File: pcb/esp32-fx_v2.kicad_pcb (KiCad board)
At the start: 4 copper layers, 48 x 95 mm, 80 parts, among them J1 AudioJack2 (out), J2 AudioJack2 (in), K1 G6E-134P-US-DC3, P1 USB_C_Plug_USB2.0, Q1 MMBT2222A, SW1 SW_Push, U1 ESP32-S3-WROOM-1, U10 OPA1655DBV, U11 D3V3XA4B10LP, U2 TPD1E05U06DYA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

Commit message: added images of pcb
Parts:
- removed the C17 at (150.8, 88.4)
- moved R1 1.40 mm to (150.8, 88.5)
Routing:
- net /U3A-OUT: track 18.9 -> 17.4 mm
- net Net-(U10-+): track 20.7 -> 19.4 mm
- net GND: vias 131 -> 132
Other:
- board text removed: "BLCK"
- board text removed: "DIN"
- board text removed: "DOUT"
- board text removed: "LRCKL"
- board text removed: "MLCK"
- board text removed: "NRST"
- board text removed: "SCL"
- board text removed: "SDA"

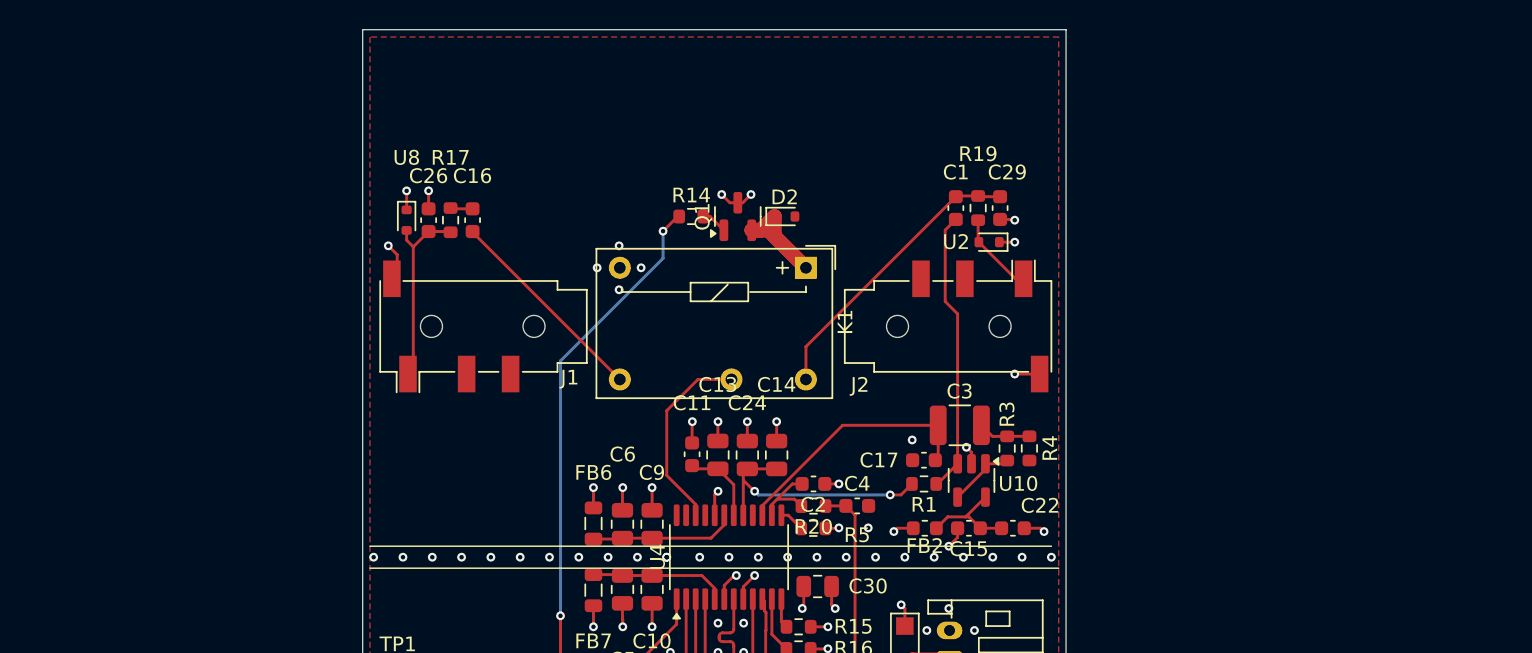
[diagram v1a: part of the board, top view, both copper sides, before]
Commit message: fixed input and output values and removed opamp
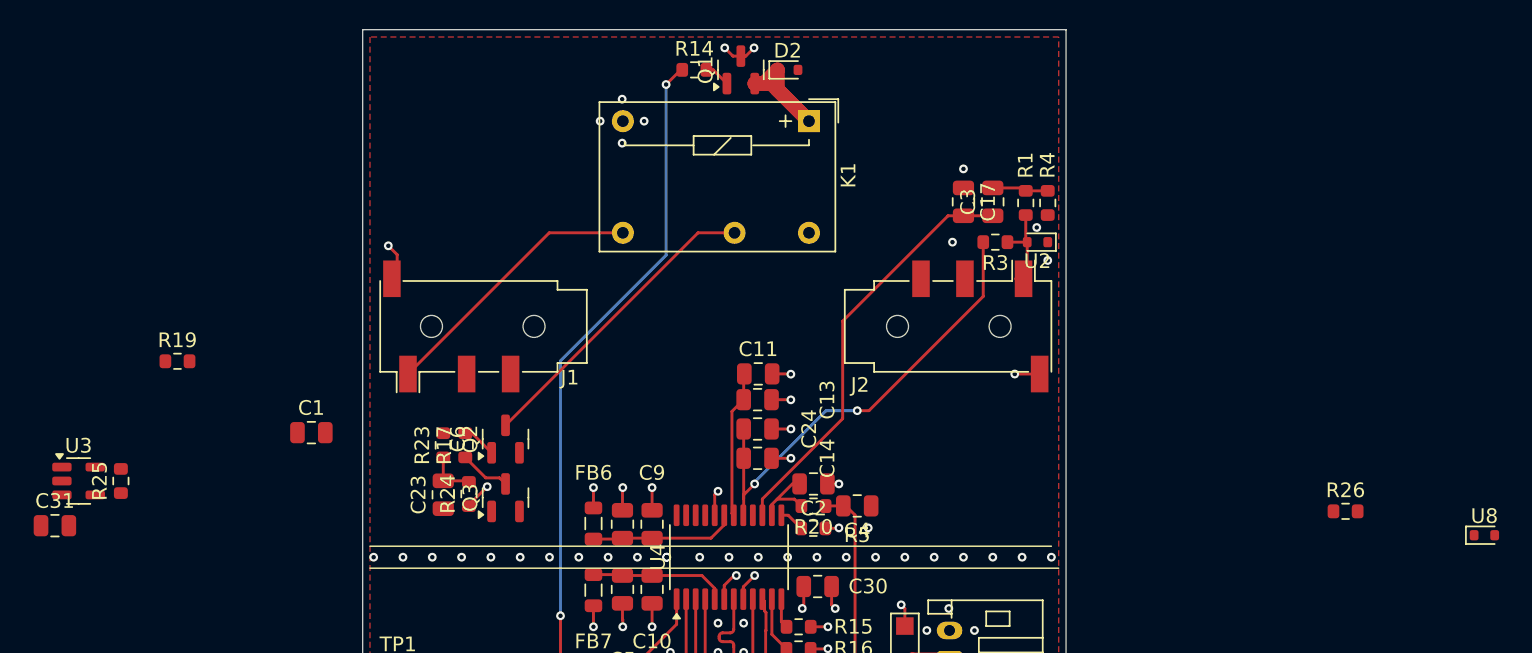
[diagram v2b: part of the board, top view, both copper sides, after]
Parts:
- removed C15, C16: 1uf, Capacitor_SMD:C_0603_1608Metric
- removed C22: 0.1uf, Capacitor_SMD:C_0603_1608Metric
- removed C26: 100pf, Capacitor_SMD:C_0603_1608Metric
- removed C29: 100nf, Capacitor_SMD:C_0603_1608Metric
- removed FB2: 600 Ω 0.06 Ω, Inductor_SMD:L_0603_1608Metric
- removed U10: OPA1655DBV, Package_TO_SOT_SMD:SOT-23-5
- added C23: 3.3uf, Capacitor_SMD:C_0805_2012Metric, F.Cu at (118.0, 89.2)
- added C31: 3.3uf, Capacitor_SMD:C_0805_2012Metric, F.Cu at (91.5, 91.3)
- added Q2: MMBT2222A, Package_TO_SOT_SMD:SOT-23, F.Cu at (122.2, 85.4)
- added Q3: MMUN2111LT1, Package_TO_SOT_SMD:SOT-23, F.Cu at (122.2, 89.4)
- added R23: 470, Resistor_SMD:R_0603_1608Metric, F.Cu at (118.0, 85.9)
- added R24: 10k, Resistor_SMD:R_0603_1608Metric, F.Cu at (119.8, 89.2)
- added R25: 10k, Resistor_SMD:R_0603_1608Metric, F.Cu at (96.0, 88.3)
- added R26: 47k, Resistor_SMD:R_0603_1608Metric, F.Cu at (179.6, 90.4)
- added U3: OPA333xxDBV, Package_TO_SOT_SMD:SOT-23-5, F.Cu at (93.1, 88.3)
- C1: value 1uf -> 1uF; footprint Capacitor_SMD:C_0603_1608Metric -> Capacitor_SMD:C_0805_2012Metric
- C11, C17, C2, C4: footprint Capacitor_SMD:C_0603_1608Metric -> Capacitor_SMD:C_0805_2012Metric
- C3: footprint Capacitor_SMD:C_1210_3225Metric -> Capacitor_SMD:C_0805_2012Metric
- R1: value 100k -> 2k
- R17: value 22 -> 2k
- R19: value 1k -> 560
- R3: value 2k -> 100k
- moved U8 76.6 mm to (189.1, 92.0), turned to 0 degrees
- moved R19 55.6 mm to (99.9, 80.1), turned to 0 degrees
- moved C1 46.6 mm to (109.0, 85.0), turned to 0 degrees
- moved R1 20.4 mm to (157.8, 69.3), turned to -90 degrees
- moved C17 17.8 mm to (153.5, 69.2), turned to -90 degrees
- moved R4 16.8 mm to (159.2, 69.3)
- moved C3 15.4 mm to (155.5, 69.2), turned to 90 degrees
- moved R17 15.4 mm to (119.5, 85.9), turned to 90 degrees
- moved R3 14.1 mm to (155.7, 72.0), turned to 180 degrees
- moved D2 10.0 mm to (141.5, 60.2)
- moved K1 10.0 mm to (143.0, 63.7)
- moved Q1 10.0 mm to (138.3, 60.2)
- moved R14 10.0 mm to (135.1, 60.2)
- moved C11 7.10 mm to (139.5, 81.0), turned to 0 degrees
- moved C13 4.64 mm to (139.4, 82.8), turned to 180 degrees
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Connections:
- C1 pad 1: Net-(U10-+) -> Net-(C1-Pad1)
- C1 pad 2: /audioINjack -> Net-(C1-Pad2)
- C27 pad 1: Net-(C27-Pad1) -> GND
- C28 pad 1: Net-(U7-VO) -> +3.3V
- C28 pad 2: +3.3V -> GND
- FB5 pad 2: Net-(C27-Pad1) -> Net-(U7-VI)
- J1 pad T: Net-(U8-GND) -> /audioOUTjack
- R1 pad 1: Net-(U10-+) -> Net-(C3-Pad2)
- R1 pad 2: /VQ -> Net-(U2-GND)
- R17 pad 2: Net-(U8-GND) -> Net-(Q2-B)
- R19 pad 1: Net-(U2-GND) -> Net-(C1-Pad2)
- R19 pad 2: /audioINjack -> /AudioOUT
- R3 pad 1: Net-(U10--) -> Net-(U2-GND)
- R3 pad 2: Net-(C3-Pad2) -> /VQ
- U4 pad 21: unconnected-(U4-~{MUTEA}-Pad21) -> /MUTE
- U4 pad 22: /AudioOUT -> Net-(U4-OUTA)
- U7 pad 2: Net-(U7-VO) -> +3.3V
- U8 pad 2: Net-(U8-GND) -> /audioOUTjack
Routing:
- net /audioINjack: track 19.8 -> 0.00 mm
- net Net-(U10-+): track 19.4 -> 0.00 mm
- net /VQ: track 17.5 -> 31.9 mm
- net Net-(U8-GND): track 13.0 -> 0.00 mm
- net /U3A-OUT: track 17.4 -> 28.7 mm
- net /relay: track 67.7 -> 77.8 mm
- net /AudioOUT: track 13.3 -> 21.1 mm
- net Net-(U10-V+): track 7.00 -> 0.00 mm
- net GND: track 79.2 -> 72.2 mm, vias 132 -> 129
- net Net-(U10--): track 4.63 -> 0.00 mm
- net Net-(U4-FIL+): track 5.47 -> 10.1 mm
- net /audioOUTjack: track 14.3 -> 18.7 mm
- net Net-(C23-Pad2): track 0.00 -> 3.38 mm
- net Net-(Q2-B): track 0.00 -> 2.35 mm
- net Net-(Q3-C): track 1.52 -> 3.50 mm
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- removed copper zone on F.Cu, net Net-(U7-VO)

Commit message: added mute layout
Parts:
- C11: value 47uf -> 10uf; footprint Capacitor_SMD:C_0805_2012Metric -> Capacitor_SMD:C_0603_1608Metric
- C13, C14: footprint Capacitor_SMD:C_0805_2012Metric -> Capacitor_SMD:C_0603_1608Metric
- C24: value 10uF -> 47uF; footprint Capacitor_SMD:C_0805_2012Metric -> Capacitor_SMD:C_0603_1608Metric
- moved U8 74.1 mm to (115.5, 83.5), turned to 180 degrees
- moved R26 56.1 mm to (123.8, 84.0)
- moved C31 32.5 mm to (124.0, 89.7), turned to -90 degrees
- moved U3 27.7 mm to (120.8, 90.2)
- moved R25 21.9 mm to (117.8, 91.0), turned to -90 degrees
- moved R19 20.2 mm to (119.6, 84.2)
- moved C23 15.1 mm to (132.8, 86.2)
- moved R23 13.1 mm to (131.1, 86.2), turned to -90 degrees
- moved D2 10.5 mm to (141.5, 70.7)
- moved K1 10.5 mm to (143.0, 74.2)
- moved Q1 10.5 mm to (138.3, 70.7)
- moved R14 10.5 mm to (135.1, 70.7)
- moved R24 10.2 mm to (129.5, 86.2), turned to -90 degrees
- moved C1 10.1 mm to (118.9, 86.7), turned to 90 degrees
- moved C11 6.35 mm to (136.0, 86.3), turned to 90 degrees
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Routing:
- net /LPF: track 0.00 -> 14.4 mm
- net Net-(Q3-C): track 3.50 -> 16.2 mm, vias 0 -> 2
- net /MUTE: track 0.00 -> 12.3 mm, vias 0 -> 2
- net /relay: track 77.8 -> 67.3 mm
- net /MUTE+: track 0.00 -> 6.44 mm, vias 0 -> 2
- net Net-(U4-OUTA): track 0.00 -> 5.33 mm
- net Net-(U4-FIL+): track 10.1 -> 5.41 mm
- net /VQ: track 31.9 -> 29.6 mm
- net /AudioOUT: track 21.1 -> 19.0 mm
- net GND: track 72.2 -> 70.2 mm, vias 129 -> 128
- net Net-(Q2-B): track 2.35 -> 4.33 mm
- net Net-(C1-Pad1): track 0.00 -> 1.88 mm
- net /MUTE-: track 0.00 -> 1.86 mm
- net Net-(C1-Pad2): track 0.00 -> 1.77 mm
- net /audioOUTjack: track 18.7 -> 19.5 mm
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
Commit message: added back opamp
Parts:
- removed R3: 100k, Resistor_SMD:R_0603_1608Metric
- added C15: 0.1uF, Capacitor_SMD:C_0805_2012Metric, F.Cu at (152.5, 91.5)
- added C16: 1uF, Capacitor_SMD:C_0805_2012Metric, F.Cu at (152.5, 89.5)
- added FB1: 100 Ω at 100 MHz, Inductor_SMD:L_0805_2012Metric, F.Cu at (149.9, 90.5)
- added U9: OPA333xxDBV, Package_TO_SOT_SMD:SOT-23-5, F.Cu at (152.5, 86.8)
- moved C17 22.5 mm to (156.8, 91.5), turned to 180 degrees
- moved C3 20.3 mm to (156.8, 89.5), turned to 0 degrees
- moved R4 18.6 mm to (156.8, 87.8), turned to 180 degrees
- moved R1 17.0 mm to (156.8, 86.2), turned to 180 degrees
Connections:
- net /VQ renamed Net-(U4-VQ)
- C17 pad 2: /U3A-OUT -> Net-(U9-+)
- C3 pad 1: /U3A-OUT -> Net-(U9-+)
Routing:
- net Net-(U4-VQ): track 29.6 -> 6.70 mm, vias 2 -> 0
- net /U3A-OUT: track 28.7 -> 17.3 mm
- net Net-(U2-GND): track 5.95 -> 15.1 mm
- net Net-(U9-+): track 0.00 -> 7.00 mm
- net GND: track 70.2 -> 73.7 mm, vias 128 -> 131
- net +3.3V: track 53.9 -> 55.6 mm, vias 18 -> 19
- net Net-(C3-Pad2): track 3.83 -> 3.30 mm

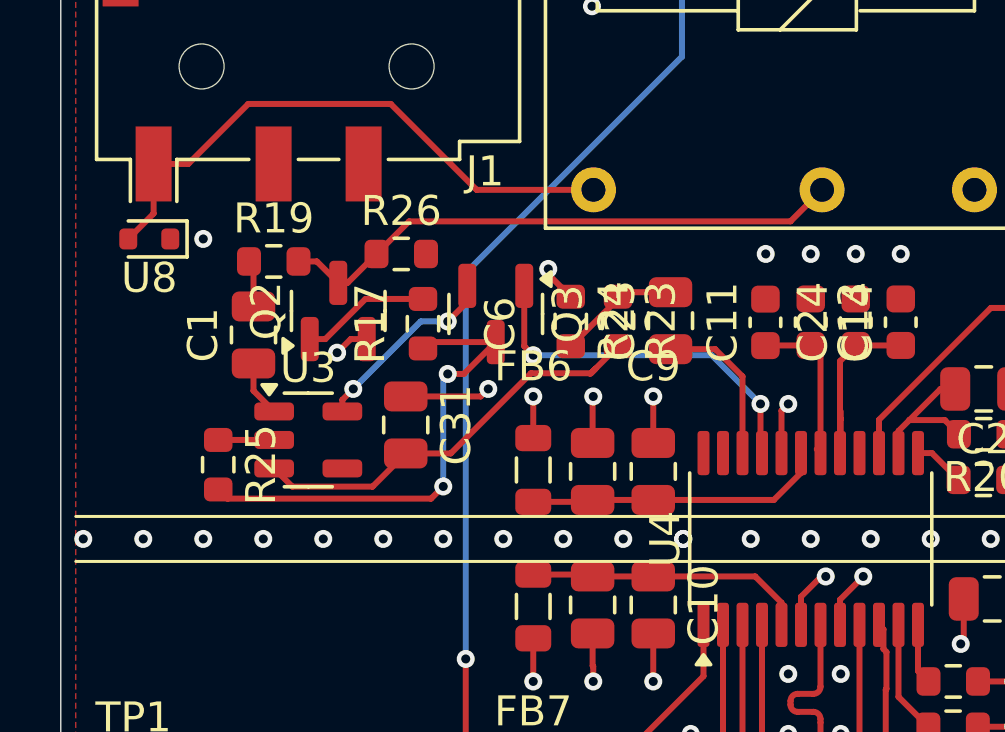
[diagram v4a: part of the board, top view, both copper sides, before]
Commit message: made opamps neater
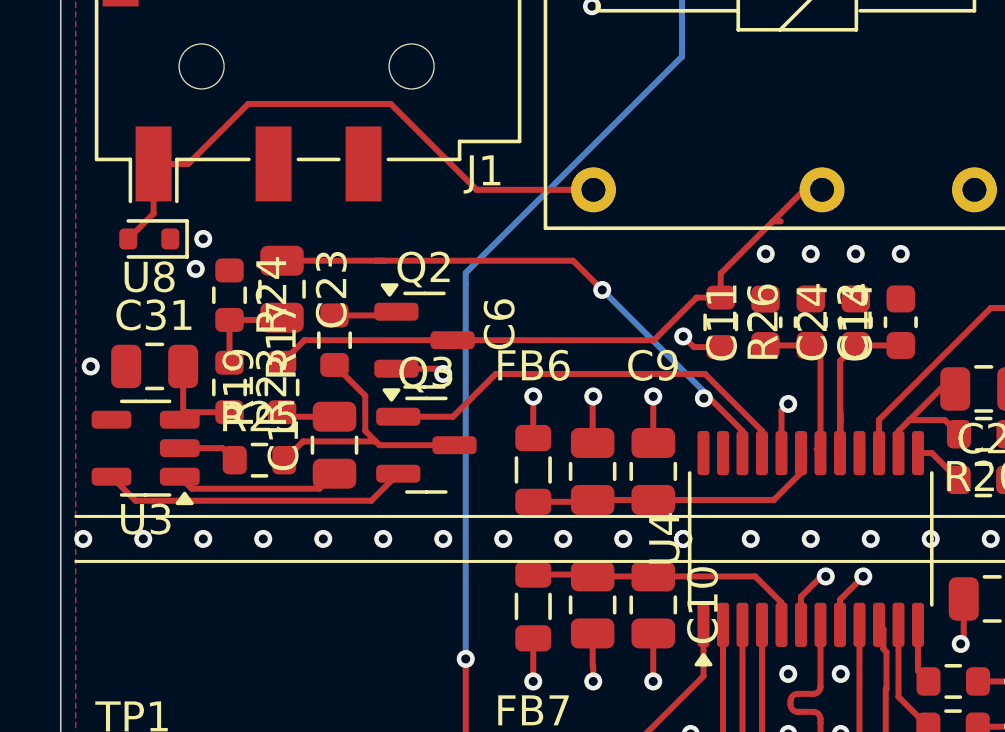
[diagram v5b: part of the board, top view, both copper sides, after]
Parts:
- moved R23 13.1 mm to (118.1, 88.5)
- moved C23 13.0 mm to (119.9, 85.2), turned to -90 degrees
- moved R24 11.4 mm to (118.1, 85.4)
- moved R26 10.9 mm to (134.5, 86.3), turned to -90 degrees
- moved C31 8.59 mm to (115.6, 87.7), turned to 0 degrees
- moved U3 5.43 mm to (115.3, 90.5), turned to 180 degrees
- moved Q3 4.95 mm to (124.7, 90.4), turned to 0 degrees
- moved C1 4.56 mm to (121.6, 90.4)
- moved R19 4.21 mm to (119.9, 88.5), turned to 90 degrees
- moved Q2 3.04 mm to (124.6, 86.9), turned to 0 degrees
- moved R17 3.00 mm to (121.6, 86.9)
- moved R25 1.38 mm to (119.1, 90.9), turned to 0 degrees
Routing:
- net Net-(U4-OUTA): track 5.33 -> 18.8 mm, vias 0 -> 2
- net /LPF: track 14.4 -> 3.58 mm
- net Net-(Q3-C): track 16.2 -> 9.11 mm, vias 2 -> 0
- net /MUTE+: track 6.44 -> 10.3 mm, vias 2 -> 0
- net Net-(C1-Pad1): track 1.88 -> 5.53 mm
- net GND: track 73.7 -> 71.5 mm, vias 131 -> 132
- net Net-(Q2-B): track 4.33 -> 2.11 mm
- net /AudioOUT: track 19.0 -> 21.1 mm
- net /MUTE: track 12.3 -> 14.2 mm, vias 2 -> 0
- net Net-(C23-Pad2): track 4.22 -> 3.21 mm

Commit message: REALLY cleaned up opamps
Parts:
- moved R24 6.51 mm to (114.4, 90.7), turned to 180 degrees
- moved C23 5.86 mm to (114.2, 86.7)
- moved R25 5.59 mm to (124.7, 91.0), turned to 90 degrees
- moved C1 5.02 mm to (118.2, 86.7)
- moved R19 4.93 mm to (124.0, 85.7), turned to 0 degrees
- moved R23 3.81 mm to (114.4, 89.2), turned to 0 degrees
- moved R17 3.27 mm to (124.7, 88.0)
- moved Q3 3.18 mm to (121.5, 90.7)
- moved Q2 3.12 mm to (121.5, 87.2)
- moved U3 2.38 mm to (117.7, 90.5), turned to -90 degrees
- moved C31 1.20 mm to (116.2, 86.7), turned to -90 degrees
- moved U8 0.95 mm to (114.5, 83.5), turned to 0 degrees
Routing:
- net /MUTE+: track 10.3 -> 1.95 mm
- net /MUTE-: track 2.00 -> 10.2 mm
- net Net-(U4-OUTA): track 18.8 -> 26.0 mm
- net Net-(U9-V+): track 0.00 -> 5.50 mm
- net Net-(Q3-C): track 9.11 -> 3.84 mm
- net GND: track 71.5 -> 75.8 mm, vias 132 -> 131
- net Net-(C1-Pad1): track 5.53 -> 1.85 mm
- net Net-(C1-Pad2): track 1.81 -> 5.32 mm
- net /MUTE: track 14.2 -> 17.5 mm, vias 0 -> 2
- net Net-(Q2-B): track 2.11 -> 5.31 mm
- net /AudioOUT: track 21.1 -> 18.4 mm
- net +3.3V: vias 19 -> 24

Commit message: editded pcb
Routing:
- net GND: vias 131 -> 138
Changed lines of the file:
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@@
 		)
 		(property "Value" "5k"
-			(at 0 1.43 90)
+			(at -0.01 1.43 90)
 			(layer "F.Fab")
 			(effects
@@
 		(tags "resistor")
 		(property "Reference" "R21"
-			(at 0 -1.43 90)
+			(at 0 1.75 90)
 			(layer "F.SilkS")
 			(effects
@@
 	)
 	(via
+		(at 143 117)
+		(size 0.6)
+		(drill 0.3)
+		(layers "F.Cu" "B.Cu")
+		(free yes)
+		(net 1)
+	)
+	(via
 		(at 155.5 93.5)
 		(size 0.6)
@@
 	)
 	(via
+		(at 141 128.5)
+		(size 0.6)
+		(drill 0.3)
+		(layers "F.Cu" "B.Cu")
+		(free yes)
+		(net 1)
+	)
+	(via
 		(at 145.5 93.5)
 		(size 0.6)
@@
 	)
 	(via
+		(at 143 128.5)
+		(size 0.6)
+		(drill 0.3)
+		(layers "F.Cu" "B.Cu")
+		(free yes)
+		(net 1)
+	)
+	(via
 		(at 153.75 142.729998)
 		(size 0.6)
@@
 	)
 	(via
+		(at 143 115)
+		(size 0.6)
+		(drill 0.3)
+		(layers "F.Cu" "B.Cu")
+		(free yes)
+		(net 1)
+	)
+	(via
 		(at 132 104.5)
 		(size 0.6)
@@
 	)
 	(via
+		(at 143 113)
+		(size 0.6)
+		(drill 0.3)
+		(layers "F.Cu" "B.Cu")
+		(free yes)
+		(net 1)
+	)
+	(via
 		(at 150 118.75)
 		(size 0.6)
@@
 	)
 	(via
+		(at 141 130.5)
+		(size 0.6)
+		(drill 0.3)
+		(layers "F.Cu" "B.Cu")
+		(free yes)
+		(net 1)
+	)
+	(via
 		(at 138.5 98)
 		(size 0.6)
@@
 	)
 	(via
+		(at 139 130.5)
+		(size 0.6)
+		(drill 0.3)
+		(layers "F.Cu" "B.Cu")
+		(free yes)
+		(net 1)
+	)
+	(via
 		(at 119.9625 87.2)
 		(size 0.6)
@@
 		(polygon
 			(pts
-				(xy 152.875 118) (xy 143.625 118) (xy 143.625 130.75) (xy 152.875 130.75)
+				(xy 152.875 118) (xy 144.125 118) (xy 144.125 130.75) (xy 152.875 130.75)
 			)
 		)
